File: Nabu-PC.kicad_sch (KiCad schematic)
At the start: 36 parts, among them J4 DIN-5, J8 DIN-5, U1 SN74LS74AN, U10 SN74LS138N, U11 SN74LS273N, U12 UA9637ACP, U13 UA9638CP, U14 TR1863P-02 or COM1863, U15 LM3900N, U16 SN74LS32N, U17 TMS4116-15NL, U18 TMS4116-15NL, U19 TMS4116-15NL, U2 TMS9918ANL, U20 TMS4116-15NL, U21 TMS4116-15NL, U22 TMS4116-15NL, U23 TMS4116-15NL, U24 TMS4116-15NL, U25 AY-3-8910, U26 74LS153, U3 SN74LS32N, U30 SN74LS241N, U31 SN74LS14N, U32 SN74LS00N, U33 SN74LS00N, U34 SN74LS348N, U35 SN74LS373N, U4 NEC_D8251AC, U40 SN74LS241N, U41 SN74LS241N, U5 SN7406N, U6 SN74LS273N, U7 SN74LS74AN, U8 SN74LS32N, U9 SN74LS32N

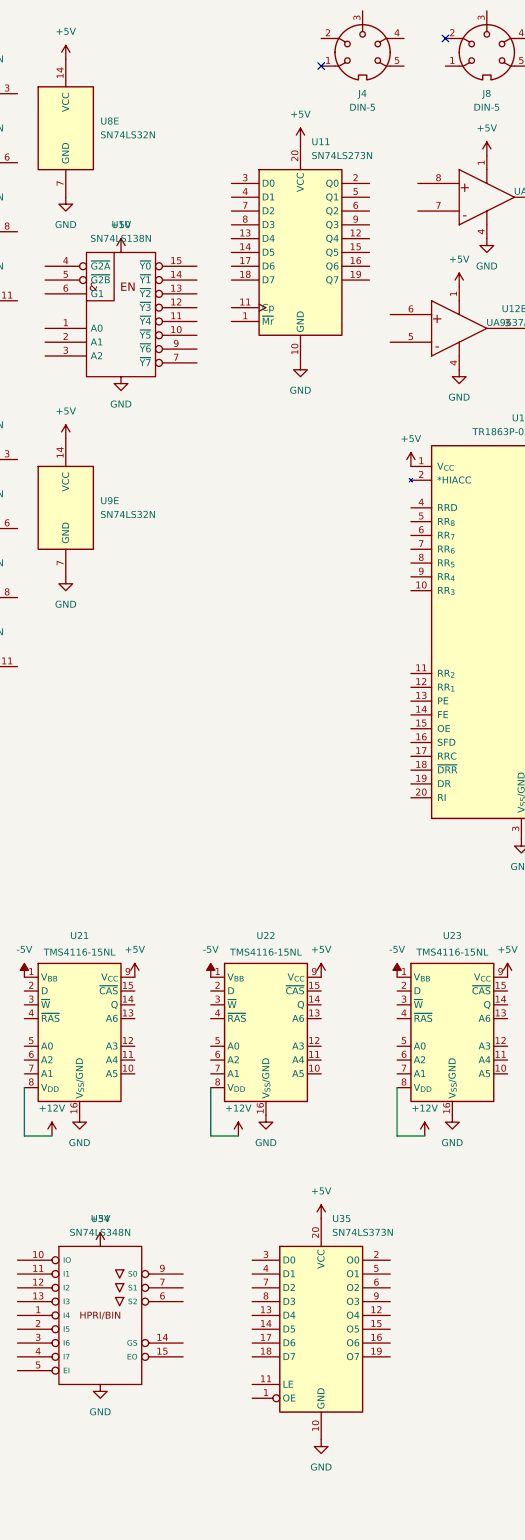
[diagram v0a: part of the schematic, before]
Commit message: Added Footprints and Datasheet for both the DIN5 Adaptor connector and DIN6 Keyboard connector.
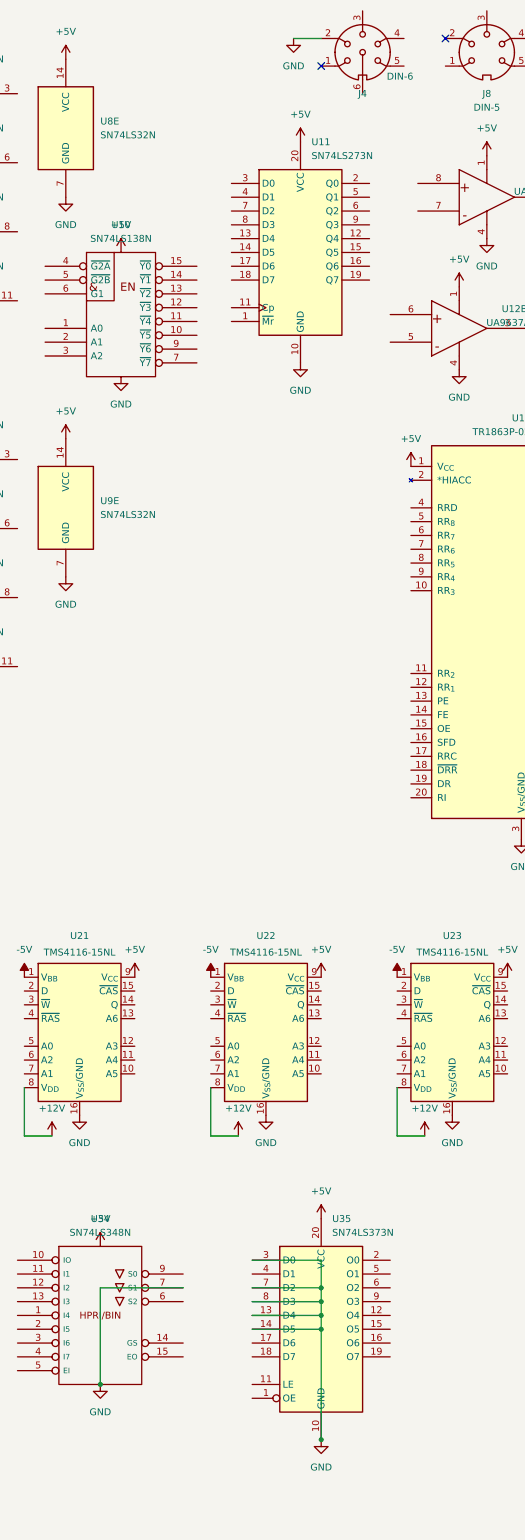
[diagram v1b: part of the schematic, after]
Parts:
- J4: value DIN-5 -> DIN-6; footprint (none) -> Nabu-PC:DIN6; symbol Connector:DIN-5 -> Connector:DIN-6
- J8: footprint (none) -> Nabu-PC:DIN5
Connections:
- net GND: now also J4.2, U34.7 (S1), U35.13 (D4), U35.14 (D5), U35.3 (D0), U35.7 (D2), U35.8 (D3)
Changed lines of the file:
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@@
     (title "Nabu PC main board.")
   )
+  (junction (at 285.75 266.7) (diameter 0) (color 0 0 0 0)
+  )
+  (junction (at 326.39 276.86) (diameter 0) (color 0 0 0 0)
+  )
+  (junction (at 326.39 248.92) (diameter 0) (color 0 0 0 0)
+  )
+  (junction (at 326.39 254) (diameter 0) (color 0 0 0 0)
+  )
+  (junction (at 326.39 256.54) (diameter 0) (color 0 0 0 0)
+  )
+  (junction (at 326.39 251.46) (diameter 0) (color 0 0 0 0)
+  )
   (no_connect (at 407.67 193.04))
   (no_connect (at 448.31 241.3))
@@
     (stroke (width 0) (type default) (color 0 0 0 0))
   )
+  (wire (pts (xy 326.39 248.92) (xy 326.39 251.46))
+    (stroke (width 0) (type default) (color 0 0 0 0))
+  )
   (wire (pts (xy 203.2 220.98) (xy 208.28 220.98))
     (stroke (width 0) (type default) (color 0 0 0 0))
   )
+  (wire (pts (xy 326.39 243.84) (xy 326.39 248.92))
+    (stroke (width 0) (type default) (color 0 0 0 0))
+  )
+  (wire (pts (xy 285.75 248.92) (xy 285.75 266.7))
+    (stroke (width 0) (type default) (color 0 0 0 0))
+  )
   (wire (pts (xy 306.07 220.98) (xy 306.07 212.09))
     (stroke (width 0) (type default) (color 0 0 0 0))
@@
     (stroke (width 0) (type default) (color 0 0 0 0))
   )
+  (wire (pts (xy 313.69 254) (xy 326.39 254))
+    (stroke (width 0) (type default) (color 0 0 0 0))
+  )
   (wire (pts (xy 340.36 220.98) (xy 340.36 212.09))
     (stroke (width 0) (type default) (color 0 0 0 0))
   )
+  (wire (pts (xy 326.39 256.54) (xy 326.39 276.86))
+    (stroke (width 0) (type default) (color 0 0 0 0))
+  )
   (wire (pts (xy 340.36 220.98) (xy 345.44 220.98))
     (stroke (width 0) (type default) (color 0 0 0 0))
@@
     (stroke (width 0) (type default) (color 0 0 0 0))
   )
+  (wire (pts (xy 313.69 243.84) (xy 326.39 243.84))
+    (stroke (width 0) (type default) (color 0 0 0 0))
+  )
   (wire (pts (xy 168.91 220.98) (xy 168.91 212.09))
     (stroke (width 0) (type default) (color 0 0 0 0))
   )
+  (wire (pts (xy 313.69 251.46) (xy 326.39 251.46))
+    (stroke (width 0) (type default) (color 0 0 0 0))
+  )
   (wire (pts (xy 374.65 220.98) (xy 379.73 220.98))
     (stroke (width 0) (type default) (color 0 0 0 0))
   )
+  (wire (pts (xy 313.69 256.54) (xy 326.39 256.54))
+    (stroke (width 0) (type default) (color 0 0 0 0))
+  )
+  (wire (pts (xy 300.99 248.92) (xy 285.75 248.92))
+    (stroke (width 0) (type default) (color 0 0 0 0))
+  )
+  (wire (pts (xy 313.69 248.92) (xy 326.39 248.92))
+    (stroke (width 0) (type default) (color 0 0 0 0))
+  )
   (wire (pts (xy 237.49 220.98) (xy 242.57 220.98))
     (stroke (width 0) (type default) (color 0 0 0 0))
   )
+  (wire (pts (xy 326.39 254) (xy 326.39 256.54))
+    (stroke (width 0) (type default) (color 0 0 0 0))
+  )
+  (wire (pts (xy 326.39 251.46) (xy 326.39 254))
+    (stroke (width 0) (type default) (color 0 0 0 0))
+  )
+  (wire (pts (xy 321.31 19.05) (xy 326.39 19.05))
+    (stroke (width 0) (type default) (color 0 0 0 0))
+  )
   (wire (pts (xy 271.78 220.98) (xy 276.86 220.98))
     (stroke (width 0) (type default) (color 0 0 0 0))
@@
     (property "Reference" "J8" (id 0) (at 356.8701 29.21 0))
     (property "Value" "DIN-5" (id 1) (at 356.8701 31.75 0))
-    (property "Footprint" "" (id 2) (at 356.87 21.59 0)
+    (property "Footprint" "Nabu-PC:DIN5" (id 2) (at 356.87 21.59 0)
       (effects (font (size 1.27 1.27)) hide)
     )
-    (property "Datasheet" "http://www.mouser.com/ds/2/18/40_c091_abd_e-75918.pdf" (id 3) (at 356.87 21.59 0)
+    (property "Datasheet" "Docs/DIN56-sds-j.pdf" (id 3) (at 356.87 21.59 0)
       (effects (font (size 1.27 1.27)) hide)
     )
@@
     (pin "9")
   )
+  (symbol (lib_id "power:GND") (at 321.31 19.05 0) (unit 1)
+    (in_bom yes) (on_board yes) (fields_autoplaced)
+    (property "Reference" "#PWR?" (id 0) (at 321.31 25.4 0)
+      (effects (font (size 1.27 1.27)) hide)
+    )
+    (property "Value" "GND" (id 1) (at 321.31 24.13 0))
+    (property "Footprint" "" (id 2) (at 321.31 19.05 0)
+      (effects (font (size 1.27 1.27)) hide)
+    )
+    (property "Datasheet" "" (id 3) (at 321.31 19.05 0)
+      (effects (font (size 1.27 1.27)) hide)
+    )
+    (pin "1")
+  )
   (symbol (lib_id "power:-5V") (at 168.91 191.77 0) (unit 1)
     (in_bom yes) (on_board yes) (fields_autoplaced)
@@
     (pin "1")
   )
-  (symbol (lib_id "Connector:DIN-5") (at 334.01 21.59 0) (unit 1)
+  (symbol (lib_id "Connector:DIN-6") (at 334.01 21.59 0) (unit 1)
     (in_bom yes) (on_board yes) (fields_autoplaced)
     (property "Reference" "J4" (id 0) (at 334.0101 29.21 0))
-    (property "Value" "DIN-5" (id 1) (at 334.0101 31.75 0))
-    (property "Footprint" "" (id 2) (at 334.01 21.59 0)
+    (property "Value" "DIN-6" (id 1) (at 338.455 26.035 0)
+      (effects (font (size 1.27 1.27)) (justify left))
+    )
+    (property "Footprint" "Nabu-PC:DIN6" (id 2) (at 334.01 21.59 0)
       (effects (font (size 1.27 1.27)) hide)
     )
-    (property "Datasheet" "http://www.mouser.com/ds/2/18/40_c091_abd_e-75918.pdf" (id 3) (at 334.01 21.59 0)
+    (property "Datasheet" "Docs/DIN56-sds-j.pdf" (id 3) (at 334.01 21.59 0)
       (effects (font (size 1.27 1.27)) hide)
     )
@@
     (pin "4")
     (pin "5")
+    (pin "6")
   )
   (symbol (lib_id "74xx:74LS14") (at 135.89 270.51 0) (unit 3)
@@
       (reference "#PWR?") (unit 1) (value "GND") (footprint "")
     )
+    (path "/ca2455c1-a469-4540-a703-36421fd3cf50"
+      (reference "#PWR?") (unit 1) (value "GND") (footprint "")
+    )
     (path "/cae1049b-9e13-4173-9b83-5133eae56295"
       (reference "#PWR?") (unit 1) (value "-5V") (footprint "")
@@
     )
     (path "/ccfd3339-2e53-4c58-8c87-31ac8088495e"
-      (reference "J4") (unit 1) (value "DIN-5") (footprint "")
+      (reference "J4") (unit 1) (value "DIN-6") (footprint "Nabu-PC:DIN6")
     )
     (path "/58b07038-35e6-408c-b3f3-07667b5d0286"
-      (reference "J8") (unit 1) (value "DIN-5") (footprint "")
+      (reference "J8") (unit 1) (value "DIN-5") (footprint "Nabu-PC:DIN5")
     )
     (path "/0b5a80d5-6bf7-469b-9e5e-e2d09d9bca4b"

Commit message: Created new symbols, updated existing symbols to simplify the layout, Added new hard to find Datasheets.  Almost done laying out all of the ICs!
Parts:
- removed unit 4 of U16
- removed unit 5 of U16
- removed unit 3 of U16
- removed unit 2 of U16
- removed unit 3 of U3
- removed unit 4 of U3
- removed unit 5 of U3
- removed unit 2 of U3
- removed unit 2 of U8
- removed unit 4 of U8
- removed unit 3 of U8
- removed unit 5 of U8
- removed unit 2 of U9
- removed unit 3 of U9
- removed unit 4 of U9
- removed unit 5 of U9
- added U27, U29, U37, U57: SN74LS32N, Package_DIP:DIP-14_W7.62mm_LongPads, symbol Nabu-PC:SN74LS32N
- added U28: SN74LS38N, Package_DIP:DIP-14_W7.62mm_LongPads, symbol 74xx:74LS38
- added U36, U58: SN74LS74AN, Package_DIP:DIP-14_W7.62mm_LongPads, symbol 74xx:74LS74
- added U38: (JBM)L-13-57, Package_DIP:DIP-14_W7.62mm_LongPads, symbol Nabu-PC:(JBM)L-13-57
- added U39: SN74LS00N, Package_DIP:DIP-14_W7.62mm_LongPads, symbol 74xx:74LS00
- added U53: HN462732, Package_DIP:DIP-28_W15.24mm_LongPads, symbol Nabu-PC:HN462732
- added U54: Z80CPU-Z8400A PS, Package_DIP:DIP-40_W25.4mm_LongPads, symbol CPU:Z80CPU
- added U55: SN74LS260N, Package_DIP:DIP-14_W7.62mm_LongPads, symbol Nabu-PC:SN74LS260N
- added U59: 74F04 PC, Package_DIP:DIP-14_W7.62mm_LongPads, symbol 74xx:74LS04
- U16, U3, U8, U9: symbol 74xx:74LS32 -> Nabu-PC:SN74LS32N
- U26: value 74LS153 -> SN74LS153N; footprint (none) -> Package_DIP:DIP-16_W7.62mm_LongPads
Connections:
- net +5V: now also U28.14 (VCC), U36.14 (VCC), U39.14 (VCC), U53.24 (V_{CC}), U55.14 (V_{CC}), U58.14 (VCC), U59.14 (VCC)
- net GND: now also U28.7 (GND), U36.7 (GND), U38.7 (GND), U39.7 (GND), U53.12 (GND), U54.29 (GND), U55.7 (GND), U58.7 (GND), U59.7 (GND)
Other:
- moved on the sheet: J8

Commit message: Finished laying out all of the chips; Added a few more Datasheets.
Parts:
- added U42, U43, U44, U45, U46, U47, U48, U49: MCM6665AP15, Package_DIP:DIP-16_W7.62mm_LongPads, symbol Nabu-PC:MCM6665AP15
- added U50: 16-1-330, Package_DIP:DIP-16_W7.62mm_LongPads, symbol Nabu-PC:16-1-330
- added U51, U52: SN74LS157N, Package_DIP:DIP-16_W7.62mm_LongPads, symbol 74xx:74LS157
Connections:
- net +5V: now also U42.8 (V_{CC}), U43.8 (V_{CC}), U44.8 (V_{CC}), U45.8 (V_{CC}), U46.8 (V_{CC}), U47.8 (V_{CC}), U48.8 (V_{CC}), U49.8 (V_{CC}), U51.16 (VCC), U52.16 (VCC)
- net GND: now also U42.16 (V_{SS}/GND), U43.16 (V_{SS}/GND), U44.16 (V_{SS}/GND), U45.16 (V_{SS}/GND), U46.16 (V_{SS}/GND), U47.16 (V_{SS}/GND), U48.16 (V_{SS}/GND), U49.16 (V_{SS}/GND), U51.8 (GND), U52.8 (GND)
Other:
- moved on the sheet: U10

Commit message: Consolidating multi symbol chips into 1 symbol; Added a missing Datasheet.
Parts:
- removed unit 5 of U31
- removed unit 2 of U31
- removed unit 7 of U31
- removed unit 6 of U31
- removed unit 4 of U31
- removed unit 3 of U31
- removed unit 5 of U32
- removed unit 4 of U32
- removed unit 3 of U32
- removed unit 2 of U32
- removed unit 2 of U33
- removed unit 5 of U33
- removed unit 3 of U33
- removed unit 4 of U33
- removed unit 2 of U39
- removed unit 3 of U39
- removed unit 5 of U39
- removed unit 4 of U39
- removed unit 2 of U59
- removed unit 4 of U59
- removed unit 5 of U59
- removed unit 3 of U59
- removed unit 6 of U59
- removed unit 7 of U59
- U12, U13: footprint Package_DIP:DIP-8_W7.62mm_LongPads -> Package_DIP:DIP-8_W7.62mm
- U31: symbol 74xx:74LS14 -> Nabu-PC:SN74LS14N
- U32, U33, U39: symbol 74xx:74LS00 -> Nabu-PC:SN74LS00N
- U59: symbol 74xx:74LS04 -> Nabu-PC:74F04
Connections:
- net +5V: now also U31.14 (V_{CC}), U32.14 (V_{CC}), U33.14 (V_{CC}), U39.14 (V_{CC}), U57.14 (V_{CC}), U59.14 (V_{CC})
- net GND: now also U31.7 (GND), U32.7 (GND), U33.7 (GND), U39.7 (GND), U57.7 (GND), U59.7 (GND)
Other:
- moved on the sheet: U27, U57
